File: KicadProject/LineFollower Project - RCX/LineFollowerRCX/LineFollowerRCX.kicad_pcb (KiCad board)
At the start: 2 copper layers, 127.4 x 100.6 mm, 12 parts, among them J1 Conn_01x11_Pin, J10 GND pinos, J2 Motor 1, J3 Motor 1, J4 Modulo bluetooth, J8 Conector sensor lateral Direi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, J9 VCC pinos, U1 ROB-14450, U2 LM7805_TO220

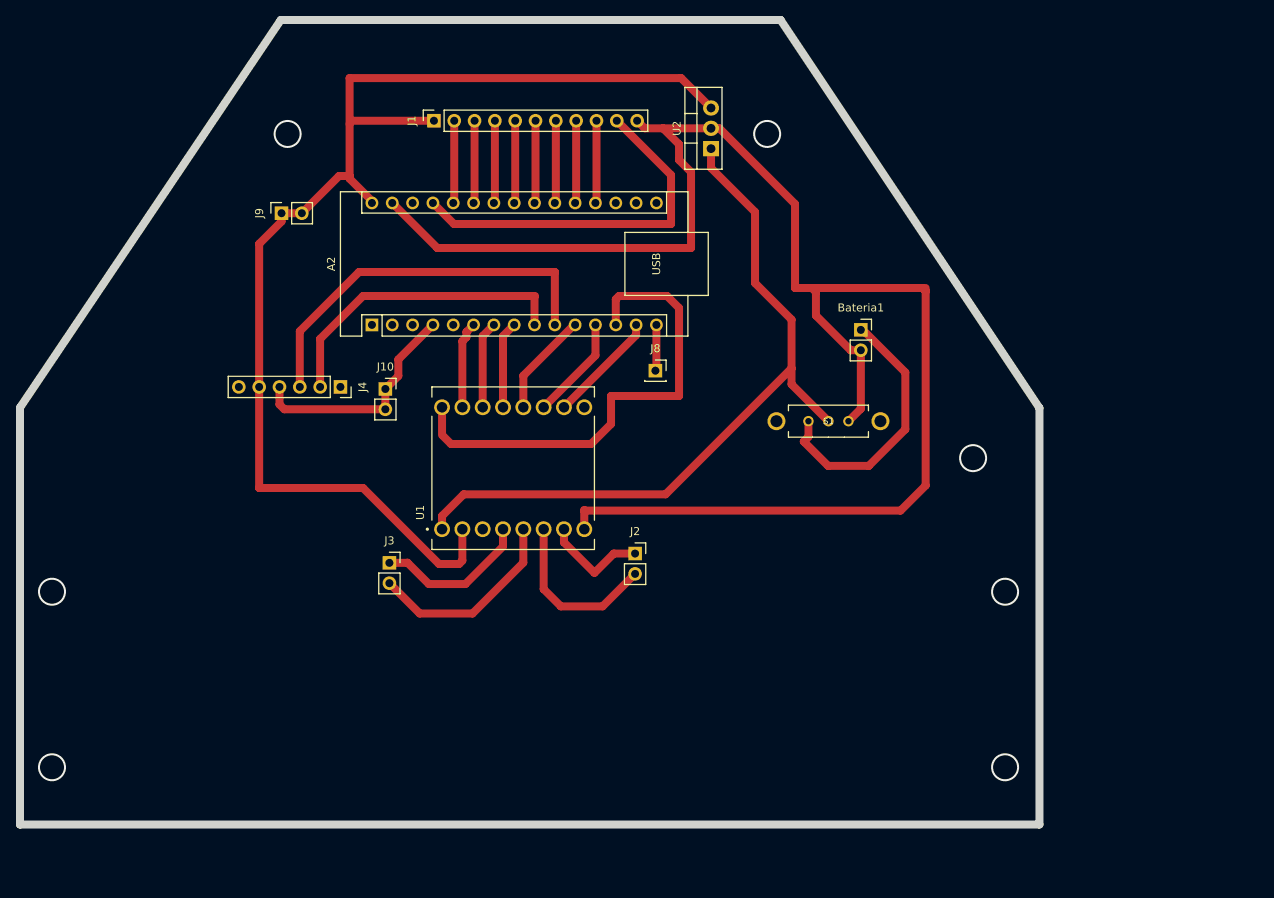
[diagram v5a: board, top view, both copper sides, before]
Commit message: tirando marcacoes e virando a placa
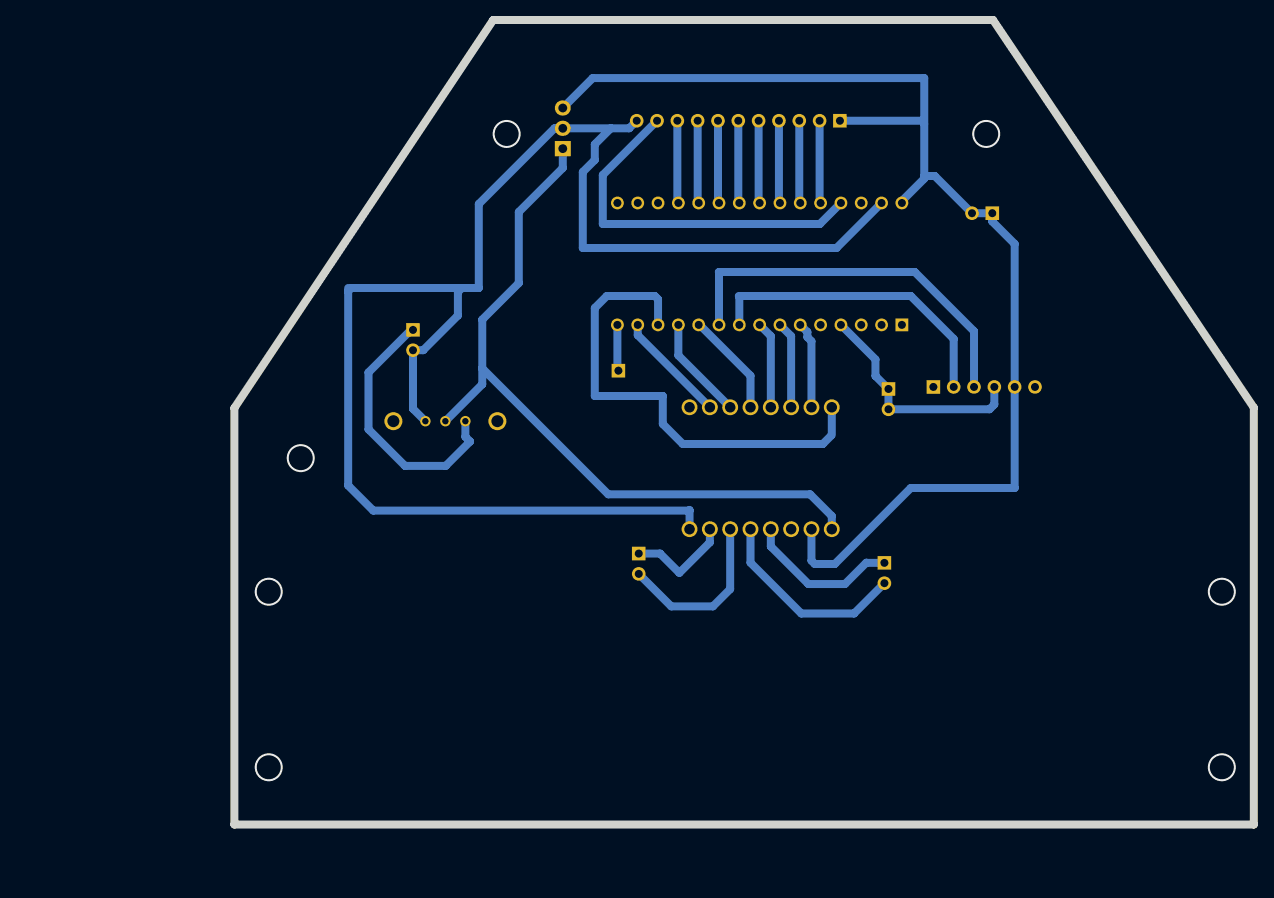
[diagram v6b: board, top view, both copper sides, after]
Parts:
- A2, Bateria1, J1, J10, J2, J3, J4, J8, J9, S1, U1, U2: moved to B.Cu
- moved J9 88.8 mm to (219.7, 78.7)
- moved J4 74.1 mm to (212.3, 100.4)
- moved A2 66.2 mm to (208.4, 92.6)
- moved J10 62.9 mm to (206.7, 100.6), turned to 180 degrees
- moved J3 61.9 mm to (206.2, 122.4), turned to 180 degrees
- moved Bateria1 56.0 mm to (147.2, 93.2), turned to 180 degrees
- moved J1 50.7 mm to (200.6, 67.1)
- moved S1 47.9 mm to (151.3, 104.6), turned to 180 degrees
- moved U1 30.9 mm to (190.7, 110.5)
- moved U2 18.5 mm to (166.0, 70.6)
- moved J8 4.62 mm to (172.9, 98.3), turned to 180 degrees
- moved J2 0.46 mm to (175.5, 121.2), turned to 180 degrees
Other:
- outline, holes or cut-outs redrawn
